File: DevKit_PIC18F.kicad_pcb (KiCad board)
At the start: 2 copper layers, 41 x 71 mm, 30 parts, among them J1 PIC_ICSP_ICD, J2 USB_C_Receptacle_USB2.0_16P, J4 RA_PORT, J5 RB_PORT, J6 RD_PORT, J7 RC_PORT, J8 RE_PORT, J9 2P_UART, SW1 SW_DIP, X1 16MHz

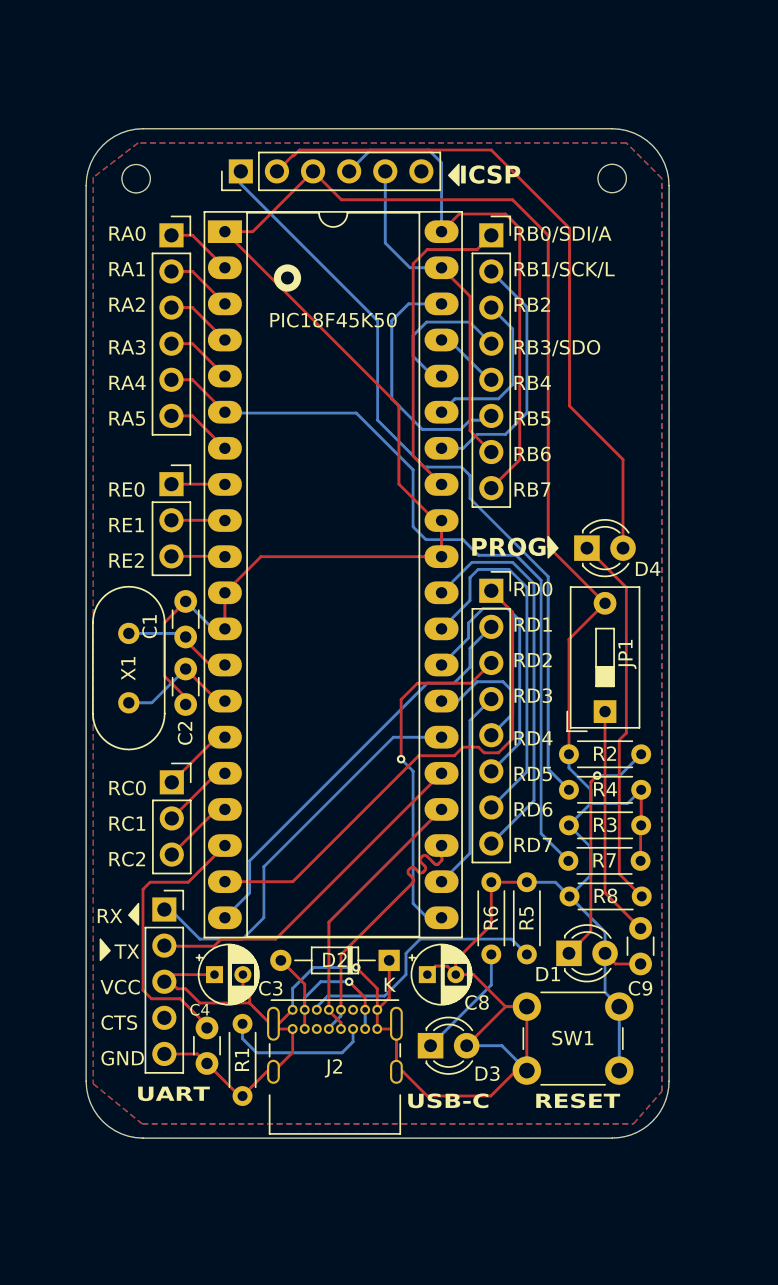
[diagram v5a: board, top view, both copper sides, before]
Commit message: Add LED/Diode-S->ICSP.
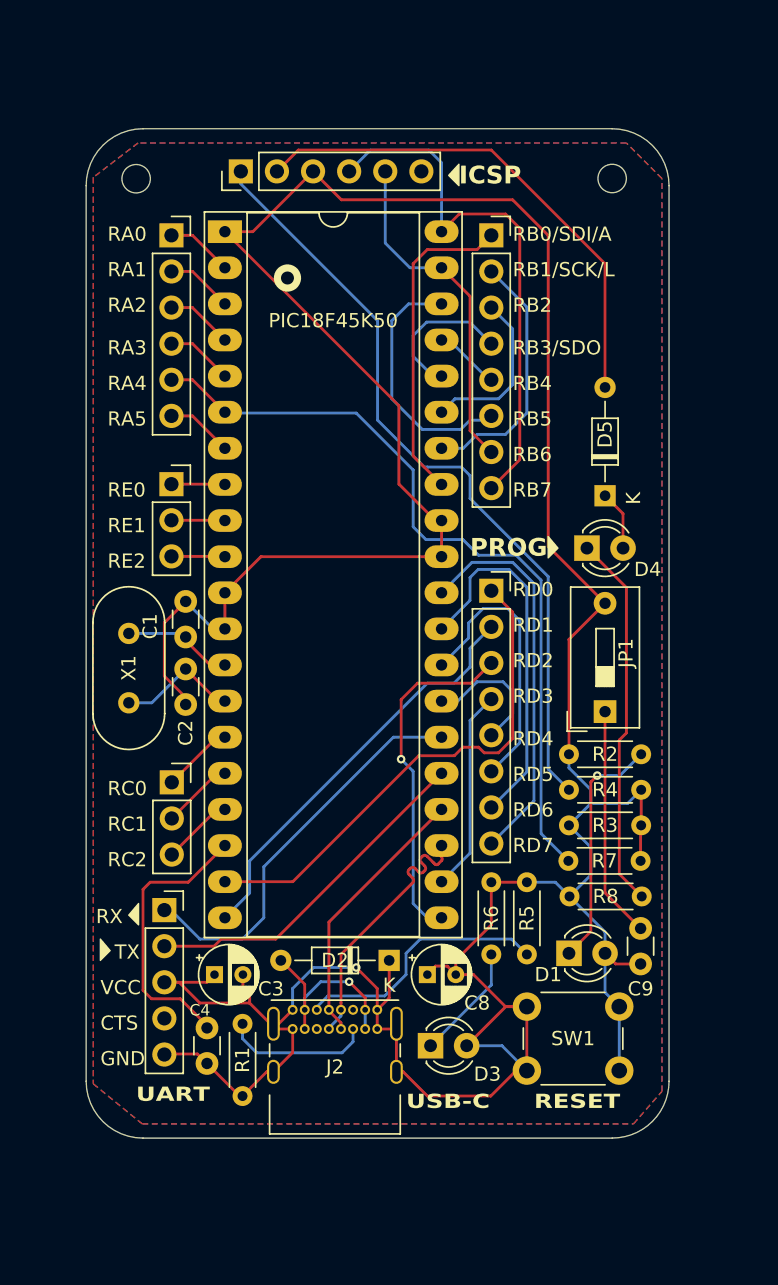
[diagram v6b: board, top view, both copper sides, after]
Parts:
- removed J9: 2P_UART, Connector_PinSocket_2.54mm:PinSocket_1x05_P2.54mm_Vertical
- added D5: D_Schottky, Diode_THT:D_DO-34_SOD68_P7.62mm_Horizontal, F.Cu at (104.5, 52.3)
- added J3: 5P_UART, Connector_PinSocket_2.54mm:PinSocket_1x05_P2.54mm_Vertical, F.Cu at (73.5, 81.5)
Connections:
- J1 pad 2: Net-(D4-A) -> Net-(D5-A)
- PIC18F45K50 pad 25: Net-(J9-Pin_2) -> /TX
- PIC18F45K50 pad 26: Net-(J9-Pin_1) -> /RX
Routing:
- net Net-(D4-A): track 47.5 -> 4.21 mm
- net Net-(D5-A): track 0.00 -> 35.7 mm
- net Net-(J9-Pin_1): track 27.8 -> 0.00 mm
- net /RX: track 0.00 -> 27.8 mm
- net Net-(J9-Pin_2): track 24.1 -> 0.00 mm
- net /TX: track 0.00 -> 24.1 mm
- net GND: track 263.2 -> 264.3 mm

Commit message: refined & ordered to fabricate test pcs.
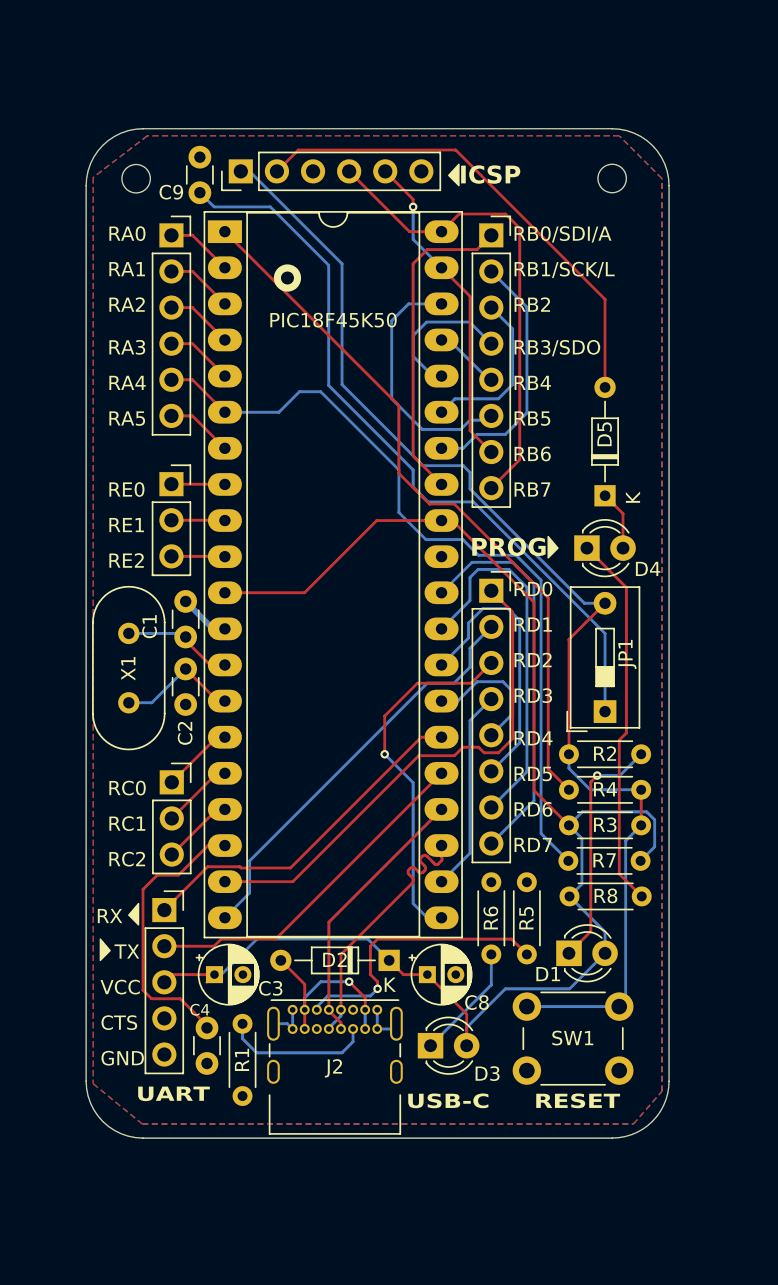
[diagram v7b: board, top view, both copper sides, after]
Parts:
- moved C9 64.7 mm to (76.0, 28.5), turned to -90 degrees
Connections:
- C3 pad 1: GND -> VCC
- C8 pad 1: GND -> VCC
- D1 pad 2: GND -> VCC
- D2 pad 1: GND -> VCC
- D3 pad 2: GND -> VCC
- J3 pad 3: GND -> VCC
- JP1 pad 2: GND -> /MCLR
- PIC18F45K50 pad 1: GND -> Net-(PIC18F45K50-RE3/VPP/*MCLR)
- PIC18F45K50 pad 11: GND -> VCC
- PIC18F45K50 pad 32: GND -> VCC
- R2 pad 2: GND -> /MCLR
- R3 pad 1: GND -> VCC
- R3 pad 2: GND -> /MCLR
- R4 pad 1: /MCLR -> Net-(PIC18F45K50-RE3/VPP/*MCLR)
- R4 pad 2: GND -> /MCLR
- R7 pad 1: GND -> VCC
- R8 pad 1: GND -> VCC
- SW1 pad 1: GND -> /MCLR
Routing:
- net GND: track 264.3 -> 11.4 mm, vias 1 -> 0
- net VCC: track 0.00 -> 105.2 mm
- net Net-(PIC18F45K50-RE3/VPP/*MCLR): track 0.00 -> 50.9 mm
- net Net-(JP1-A): track 16.3 -> 52.5 mm
- net /MCLR: track 54.6 -> 85.6 mm
- net /PGD: track 37.9 -> 33.8 mm
- net /RX: track 27.8 -> 24.6 mm
- net Net-(J2-CC1): track 18.3 -> 19.9 mm, vias 0 -> 1
- net Net-(D5-A): track 35.7 -> 34.2 mm
- net /PGC: track 24.1 -> 22.8 mm, vias 0 -> 1
- net Net-(J6-Pin_3): track 24.5 -> 25.5 mm
- net Net-(J4-Pin_5): track 54.8 -> 55.4 mm
- added copper zone on B.Cu, net GND
- removed copper zone on B.Cu, net (none)

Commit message: Switch USB-C -> USB-B for availability.
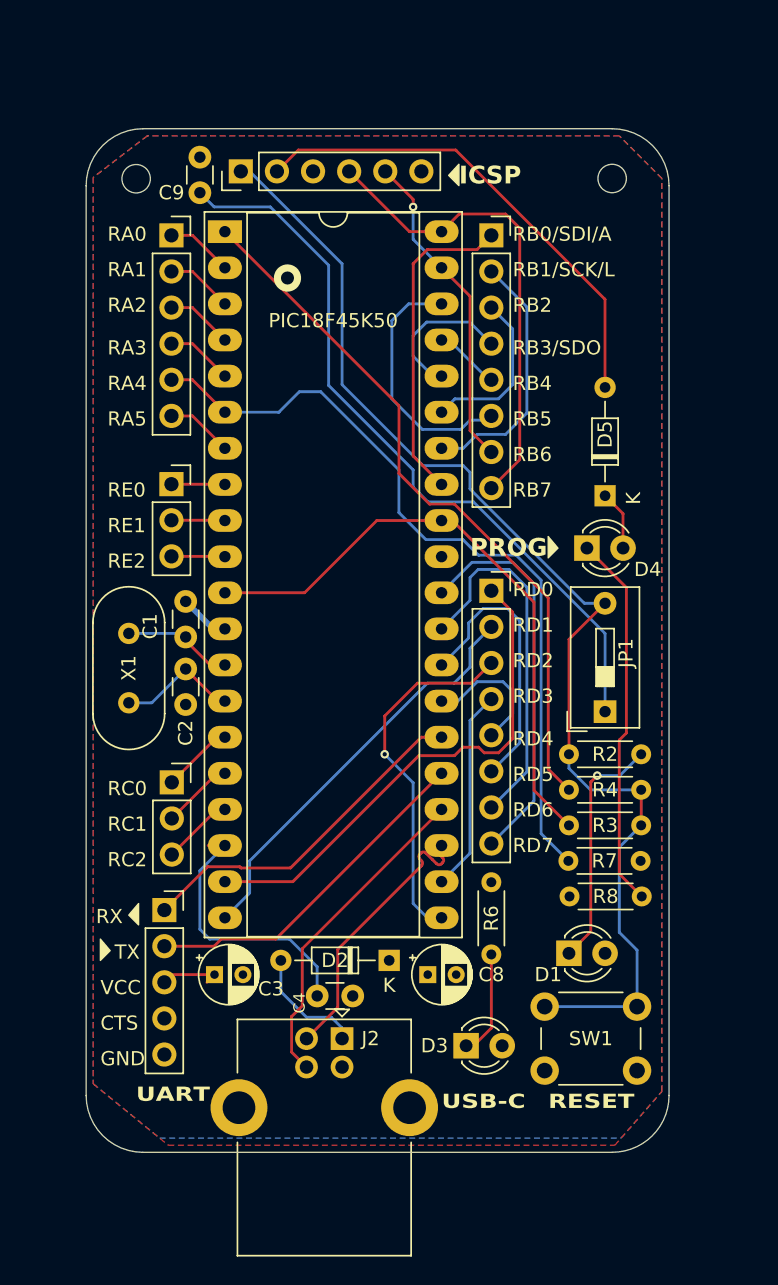
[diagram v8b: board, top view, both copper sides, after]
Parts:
- removed R1, R5: 5.1k, Resistor_THT:R_Axial_DIN0204_L3.6mm_D1.6mm_P5.08mm_Horizontal
- J2: value USB_C_Receptacle_USB2.0_16P -> USB_B; footprint Connector_USB:USB_C_Receptacle_GCT_USB4085 -> Connector_USB:USB_B_Lumberg_2411_02_Horizontal
- moved C4 11.3 mm to (86.8, 87.5), turned to 180 degrees
- moved J2 4.02 mm to (86.0, 90.5), turned to -90 degrees
- moved D3 2.50 mm to (94.7, 91.0)
- moved SW1 1.25 mm to (100.2, 88.2)
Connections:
- C3 pad 1: VCC -> GND
- C8 pad 1: VCC -> GND
- D1 pad 2: VCC -> GND
- D2 pad 1: VCC -> GND
- D3 pad 2: VCC -> GND
- J3 pad 3: VCC -> GND
- PIC18F45K50 pad 11: VCC -> GND
- PIC18F45K50 pad 32: VCC -> GND
- R3 pad 1: VCC -> GND
- R7 pad 1: VCC -> GND
- R8 pad 1: VCC -> GND
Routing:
- net VCC: track 105.2 -> 0.00 mm
- net GND: track 11.4 -> 53.2 mm
- net Net-(J2-CC1): track 19.9 -> 0.00 mm, vias 1 -> 0
- net Net-(J2-CC2): track 10.5 -> 0.00 mm
- net Net-(D2-A): track 13.8 -> 8.31 mm, vias 1 -> 0
- net /D+: track 19.1 -> 22.9 mm
- net /D-: track 19.2 -> 20.5 mm
- net Net-(D3-K): track 8.19 -> 7.31 mm
- net Net-(PIC18F45K50-VUSB3V3): track 20.6 -> 19.9 mm
- net /MCLR: track 85.6 -> 86.1 mm
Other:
- board size 41 x 71 mm -> 41 x 72 mm
